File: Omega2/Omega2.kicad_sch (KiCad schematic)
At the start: 6 parts, among them SW1 SW_DIP_x01, U1 Omega2+

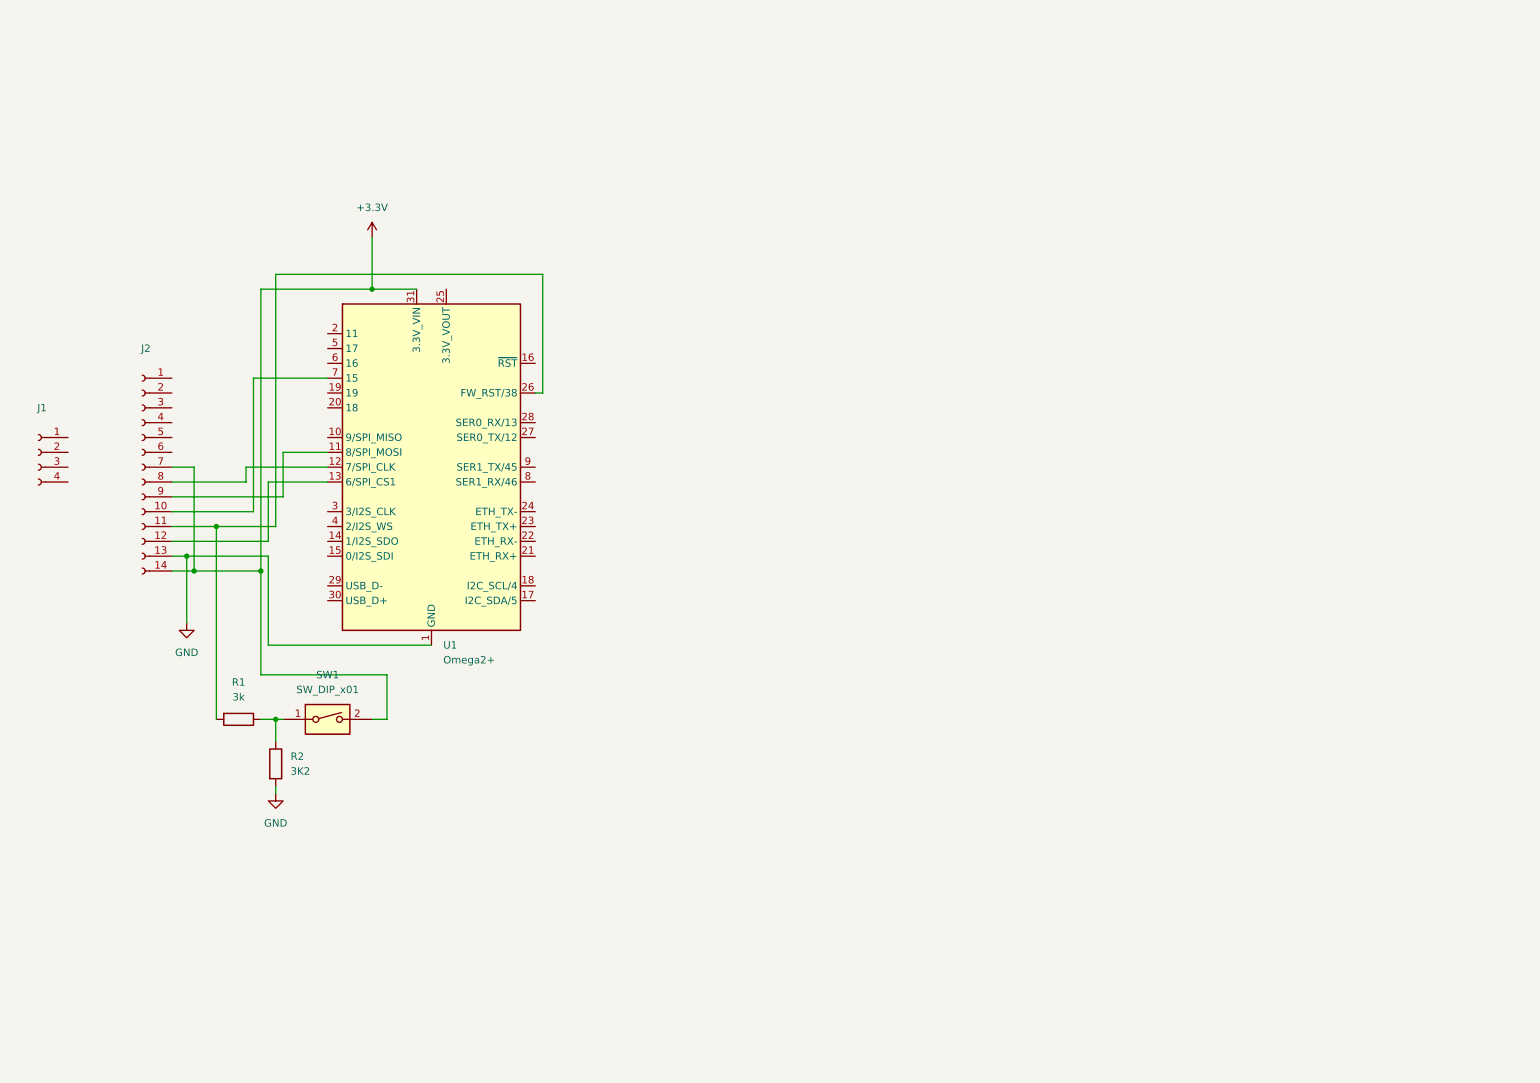
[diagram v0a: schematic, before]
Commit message: Organización display, botón de reset, power flag
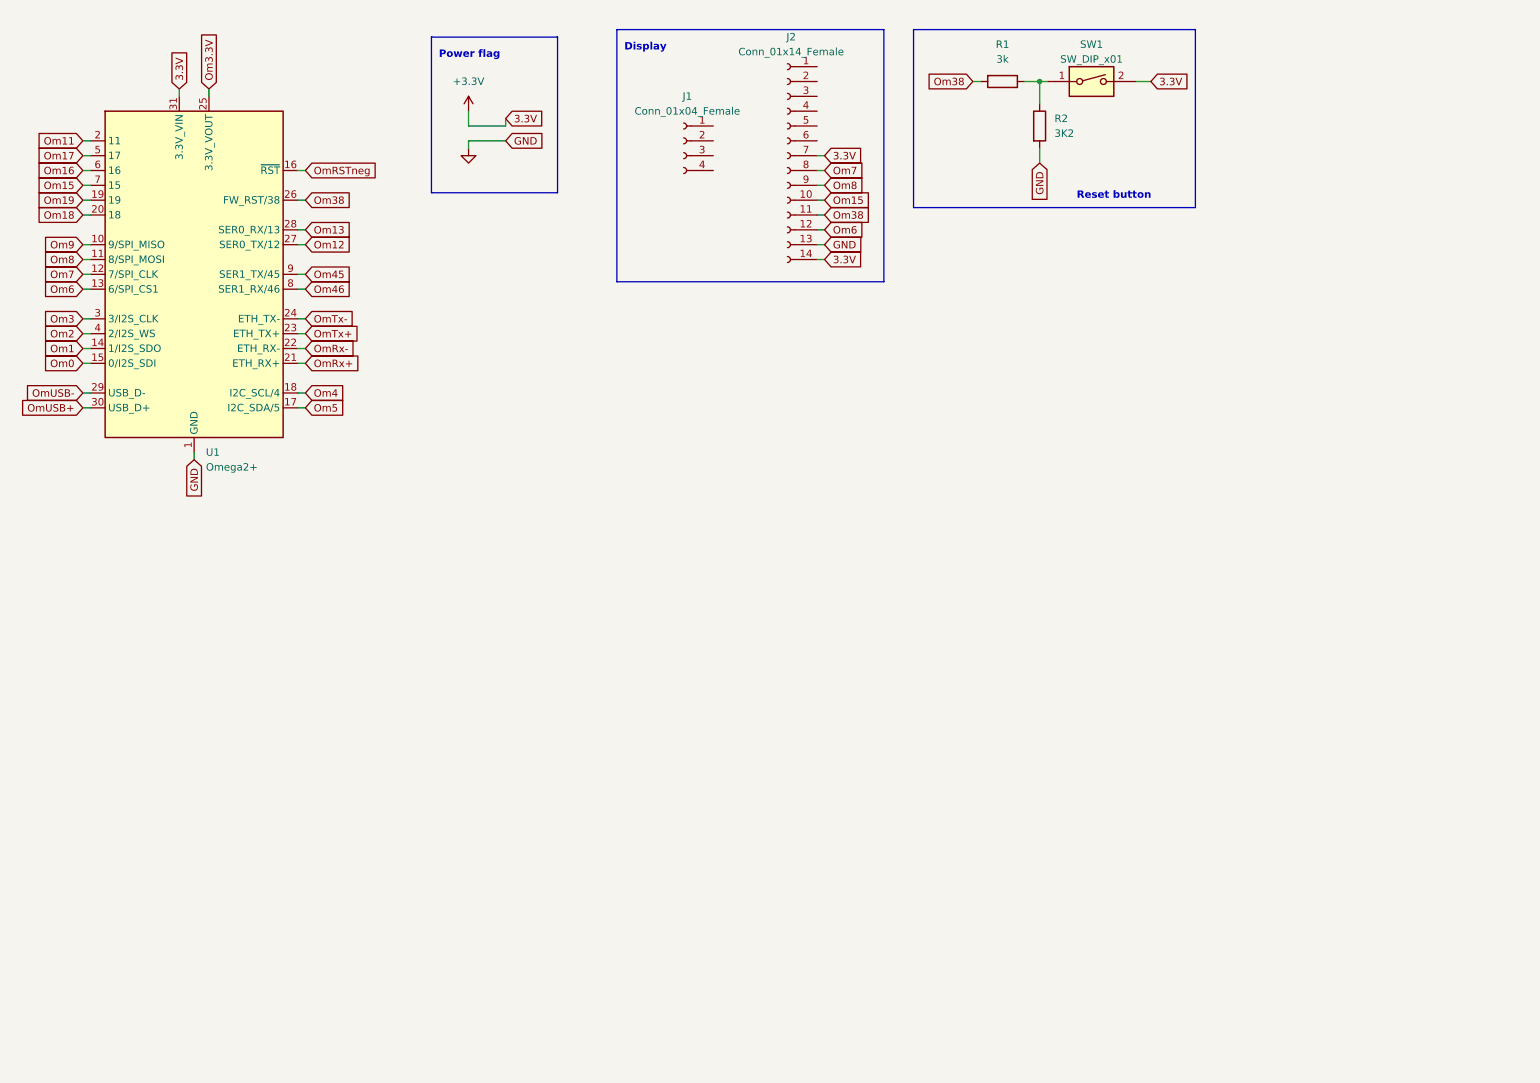
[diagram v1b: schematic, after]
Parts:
- J1: value (none) -> Conn_01x04_Female; footprint (none) -> Connector_PinSocket_2.54mm:PinSocket_1x04_P2.54mm_Vertical
- J2: value (none) -> Conn_01x14_Female; footprint (none) -> Connector_PinSocket_2.54mm:PinSocket_1x14_P2.54mm_Vertical
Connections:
- net Om15: now reaches J2.10 (Pin_10), U1.7 (15)
- net Om38: now reaches J2.11 (Pin_11), R1.2, U1.26 (FW_RST/38)
- net Om6: now reaches J2.12 (Pin_12), U1.13 (6/SPI_CS1)
- net Om7: now reaches J2.8 (Pin_8), U1.12 (7/SPI_CLK)
- net Om8: now reaches J2.9 (Pin_9), U1.11 (8/SPI_MOSI)
- net Om9: now reaches U1.10 (9/SPI_MISO)
- net Om1: now reaches U1.14 (1/I2S_SDO)
- net Om0: now reaches U1.15 (0/I2S_SDI)
- net OmRSTneg: now reaches U1.16 (~{RST})
- net Om5: now reaches U1.17 (I2C_SDA/5)
- net Om4: now reaches U1.18 (I2C_SCL/4)
- net Om19: now reaches U1.19
- net Om11: now reaches U1.2 (11)
- net Om18: now reaches U1.20 (18)
- net OmRx+: now reaches U1.21 (ETH_RX+)
- net OmRx-: now reaches U1.22 (ETH_RX-)
- net OmTx+: now reaches U1.23 (ETH_TX+)
- net OmTx-: now reaches U1.24 (ETH_TX-)
- net Om3.3V: now reaches U1.25 (3.3V_VOUT)
- net Om12: now reaches U1.27 (SER0_TX/12)
- net Om13: now reaches U1.28 (SER0_RX/13)
- net OmUSB-: now reaches U1.29 (USB_D-)
- net Om3: now reaches U1.3 (3/I2S_CLK)
- net OmUSB+: now reaches U1.30 (USB_D+)
- net Om2: now reaches U1.4 (2/I2S_WS)
- net Om17: now reaches U1.5 (17)
- net Om16: now reaches U1.6 (16)
- net Om46: now reaches U1.8 (SER1_RX/46)
- net Om45: now reaches U1.9 (SER1_TX/45)
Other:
- note added: "Display"
- note added: "Power flag"
- note added: "Reset button"
- moved on the sheet: J1, J2, R1, R2, SW1, U1

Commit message: Adicion botones
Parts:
- added C? (x2): 100n, Capacitor_SMD:C_0805_2012Metric_Pad1.18x1.45mm_HandSolder, symbol Device:C
- added R? (x2): 5.1k, Resistor_SMD:R_0805_2012Metric_Pad1.20x1.40mm_HandSolder, symbol Device:R
- added R? (x2): 51k, Resistor_SMD:R_0805_2012Metric_Pad1.20x1.40mm_HandSolder, symbol Device:R
- added SW? (x2): BT, Button_Switch_SMD:SW_SPST_EVQQ2, symbol Switch:SW_Push
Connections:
- net +3V3: now also R?.2, R?.2
- net GND: now also C?.1, C?.1, SW?.2, SW?.2
- net Om16: now also C?.2, R?.1, R?.1
- net Om17: now also C?.2, R?.1, R?.1
- new net: R?.2, SW?.1 (x2)
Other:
- note added: "Botones"

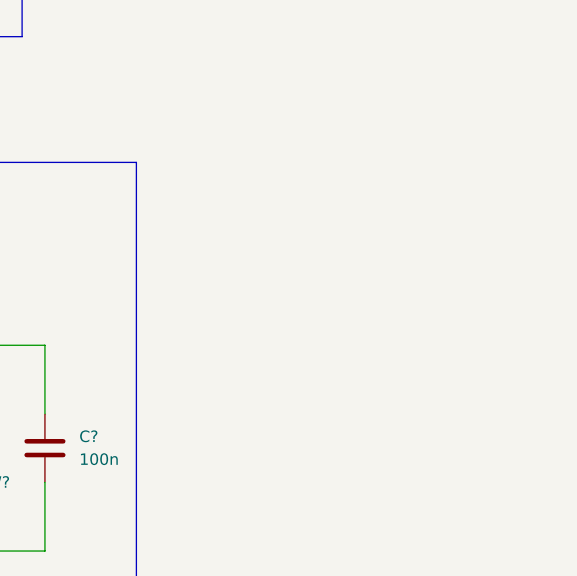
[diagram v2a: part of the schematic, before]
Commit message: Adición Teclado
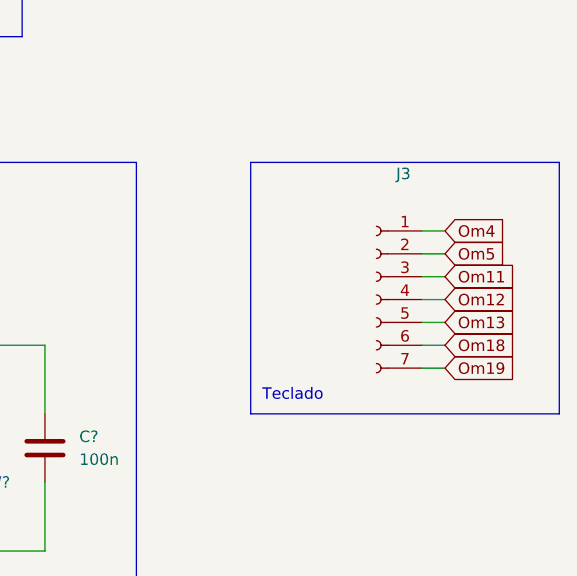
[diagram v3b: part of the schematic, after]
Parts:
- added J3: (no value), symbol Connector:Conn_01x07_Female
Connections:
- net Om11: now also J3.3 (Pin_3)
- net Om12: now also J3.4 (Pin_4)
- net Om13: now also J3.5 (Pin_5)
- net Om18: now also J3.6 (Pin_6)
- net Om19: now also J3.7 (Pin_7)
- net Om4: now also J3.1 (Pin_1)
- net Om5: now also J3.2 (Pin_2)
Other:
- note added: "Teclado"
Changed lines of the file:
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@@
   (junction (at 160.02 93.98) (diameter 0) (color 0 0 0 0)
   )
+  (wire (pts (xy 213.36 86.36) (xy 215.9 86.36))
+    (stroke (width 0) (type default) (color 0 0 0 0))
+  )
   (wire (pts (xy 97.79 33.02) (xy 104.14 33.02))
     (stroke (width 0) (type default) (color 0 0 0 0))
@@
     (stroke (width 0) (type default) (color 0 0 0 0))
   )
+  (wire (pts (xy 213.36 88.9) (xy 215.9 88.9))
+    (stroke (width 0) (type default) (color 0 0 0 0))
+  )
   (wire (pts (xy 53.34 26.67) (xy 53.34 27.94))
     (stroke (width 0) (type default) (color 0 0 0 0))
@@
     (stroke (width 0) (type default) (color 0 0 0 0))
   )
+  (wire (pts (xy 213.36 91.44) (xy 215.9 91.44))
+    (stroke (width 0) (type default) (color 0 0 0 0))
+  )
+  (wire (pts (xy 213.36 93.98) (xy 215.9 93.98))
+    (stroke (width 0) (type default) (color 0 0 0 0))
+  )
+  (wire (pts (xy 213.36 81.28) (xy 215.9 81.28))
+    (stroke (width 0) (type default) (color 0 0 0 0))
+  )
   (wire (pts (xy 69.85 50.8) (xy 68.58 50.8))
     (stroke (width 0) (type default) (color 0 0 0 0))
@@
     (stroke (width 0) (type default) (color 0 0 0 0))
   )
+  (polyline (pts (xy 228.6 101.6) (xy 194.31 101.6))
+    (stroke (width 0) (type default) (color 0 0 0 0))
+  )
   (polyline (pts (xy 109.22 73.66) (xy 181.61 73.66))
     (stroke (width 0) (type default) (color 0 0 0 0))
@@
     (stroke (width 0) (type default) (color 0 0 0 0))
   )
+  (wire (pts (xy 213.36 96.52) (xy 215.9 96.52))
+    (stroke (width 0) (type default) (color 0 0 0 0))
+  )
   (polyline (pts (xy 168.91 16.51) (xy 168.91 59.69))
     (stroke (width 0) (type default) (color 0 0 0 0))
@@
     (stroke (width 0) (type default) (color 0 0 0 0))
   )
+  (wire (pts (xy 213.36 83.82) (xy 215.9 83.82))
+    (stroke (width 0) (type default) (color 0 0 0 0))
+  )
   (wire (pts (xy 160.02 93.98) (xy 160.02 96.52))
     (stroke (width 0) (type default) (color 0 0 0 0))
@@
     (stroke (width 0) (type default) (color 0 0 0 0))
   )
+  (polyline (pts (xy 194.31 73.66) (xy 228.6 73.66))
+    (stroke (width 0) (type default) (color 0 0 0 0))
+  )
   (wire (pts (xy 195.58 25.4) (xy 196.85 25.4))
     (stroke (width 0) (type default) (color 0 0 0 0))
   )
+  (polyline (pts (xy 228.6 73.66) (xy 228.6 101.6))
+    (stroke (width 0) (type default) (color 0 0 0 0))
+  )
   (wire (pts (xy 128.27 93.98) (xy 139.7 93.98))
+    (stroke (width 0) (type default) (color 0 0 0 0))
+  )
+  (polyline (pts (xy 194.31 101.6) (xy 194.31 73.66))
     (stroke (width 0) (type default) (color 0 0 0 0))
   )
@@
     (effects (font (size 1.27 1.27)) (justify left bottom))
   )
+  (text "Teclado\n" (at 195.58 100.33 0)
+    (effects (font (size 1.27 1.27)) (justify left bottom))
+  )
   (text "Display" (at 124.46 20.32 0)
     (effects (font (size 1.27 1.27) (thickness 0.254) bold) (justify left bottom))
@@
     )
   )
+  (global_label "Om19" (shape input) (at 215.9 96.52 0) (fields_autoplaced)
+    (effects (font (size 1.27 1.27)) (justify left))
+    (property "Intersheet References" "${INTERSHEET_REFS}" (id 0) (at 223.756 96.4406 0)
+      (effects (font (size 1.27 1.27)) (justify left) hide)
+    )
+  )
+  (global_label "Om13" (shape input) (at 215.9 91.44 0) (fields_autoplaced)
+    (effects (font (size 1.27 1.27)) (justify left))
+    (property "Intersheet References" "${INTERSHEET_REFS}" (id 0) (at 223.756 91.3606 0)
+      (effects (font (size 1.27 1.27)) (justify left) hide)
+    )
+  )
   (global_label "Om3" (shape input) (at 31.75 66.04 180) (fields_autoplaced)
     (effects (font (size 1.27 1.27)) (justify right))
@@
     )
   )
+  (global_label "Om12" (shape input) (at 215.9 88.9 0) (fields_autoplaced)
+    (effects (font (size 1.27 1.27)) (justify left))
+    (property "Intersheet References" "${INTERSHEET_REFS}" (id 0) (at 223.756 88.8206 0)
+      (effects (font (size 1.27 1.27)) (justify left) hide)
+    )
+  )
   (global_label "OmUSB-" (shape input) (at 31.75 78.74 180) (fields_autoplaced)
     (effects (font (size 1.27 1.27)) (justify right))
@@
     )
   )
+  (global_label "Om5" (shape input) (at 215.9 83.82 0) (fields_autoplaced)
+    (effects (font (size 1.27 1.27)) (justify left))
+    (property "Intersheet References" "${INTERSHEET_REFS}" (id 0) (at 222.5464 83.7406 0)
+      (effects (font (size 1.27 1.27)) (justify left) hide)
+    )
+  )
   (global_label "Om7" (shape input) (at 31.75 58.42 180) (fields_autoplaced)
     (effects (font (size 1.27 1.27)) (justify right))
@@
     )
   )
+  (global_label "Om18" (shape input) (at 215.9 93.98 0) (fields_autoplaced)
+    (effects (font (size 1.27 1.27)) (justify left))
+    (property "Intersheet References" "${INTERSHEET_REFS}" (id 0) (at 223.756 93.9006 0)
+      (effects (font (size 1.27 1.27)) (justify left) hide)
+    )
+  )
   (global_label "Om6" (shape input) (at 31.75 60.96 180) (fields_autoplaced)
     (effects (font (size 1.27 1.27)) (justify right))
@@
     )
   )
+  (global_label "Om11" (shape input) (at 215.9 86.36 0) (fields_autoplaced)
+    (effects (font (size 1.27 1.27)) (justify left))
+    (property "Intersheet References" "${INTERSHEET_REFS}" (id 0) (at 223.756 86.2806 0)
+      (effects (font (size 1.27 1.27)) (justify left) hide)
+    )
+  )
   (global_label "3.3V" (shape input) (at 158.75 55.88 0) (fields_autoplaced)
     (effects (font (size 1.27 1.27)) (justify left))
     (property "Intersheet References" "${INTERSHEET_REFS}" (id 0) (at 165.2755 55.8006 0)
+      (effects (font (size 1.27 1.27)) (justify left) hide)
+    )
+  )
+  (global_label "Om4" (shape input) (at 215.9 81.28 0) (fields_autoplaced)
+    (effects (font (size 1.27 1.27)) (justify left))
+    (property "Intersheet References" "${INTERSHEET_REFS}" (id 0) (at 222.5464 81.2006 0)
       (effects (font (size 1.27 1.27)) (justify left) hide)
     )
@@
     (pin "2")
   )
+  (symbol (lib_id "Connector:Conn_01x07_Female") (at 208.28 88.9 0) (mirror y) (unit 1)
+    (in_bom yes) (on_board yes)
+    (property "Reference" "J3" (id 0) (at 212.09 74.93 0)
+      (effects (font (size 1.27 1.27)) (justify left))
+    )
+    (property "Value" "" (id 1) (at 215.9 77.47 0)
+      (effects (font (size 1.27 1.27)) (justify left))
+    )
+    (property "Footprint" "" (id 2) (at 208.28 88.9 0)
+      (effects (font (size 1.27 1.27)) hide)
+    )
+    (property "Datasheet" "~" (id 3) (at 208.28 88.9 0)
+      (effects (font (size 1.27 1.27)) hide)
+    )
+    (pin "1")
+    (pin "2")
+    (pin "3")
+    (pin "4")
+    (pin "5")
+    (pin "6")
+    (pin "7")
+  )
   (symbol (lib_id "Device:C") (at 139.7 105.41 180) (unit 1)
     (in_bom yes) (on_board yes) (fields_autoplaced)
@@
       (reference "J2") (unit 1) (value "Conn_01x14_Female") (footprint "Connector_PinSocket_2.54mm:PinSocket_1x14_P2.54mm_Vertical")
     )
+    (path "/6f4c06dc-e24f-4f66-84b3-0dc17375c4c4"
+      (reference "J3") (unit 1) (value "Conn_01x07_Female") (footprint "Connector_PinSocket_2.54mm:PinSocket_1x07_P2.54mm_Vertical")
+    )
     (path "/5c9c653f-d9af-4652-b5e1-fa03e9583f41"

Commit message: edición pulsadores
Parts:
- J3: value (none) -> Conn_01x07_Female; footprint (none) -> Connector_PinSocket_2.54mm:PinSocket_1x07_P2.54mm_Vertical
- SW2, SW3: renamed from SW?; value BT -> (none); footprint Button_Switch_SMD:SW_SPST_EVQQ2 -> (none)
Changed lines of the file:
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@@
   (symbol (lib_id "Switch:SW_Push") (at 160.02 110.49 270) (unit 1)
     (in_bom yes) (on_board yes) (fields_autoplaced)
-    (property "Reference" "SW?" (id 0) (at 163.83 109.2199 90)
-      (effects (font (size 1.27 1.27)) (justify left))
-    )
-    (property "Value" "BT" (id 1) (at 163.83 111.7599 90)
-      (effects (font (size 1.27 1.27)) (justify left))
-    )
-    (property "Footprint" "Button_Switch_SMD:SW_SPST_EVQQ2" (id 2) (at 165.1 110.49 0)
+    (property "Reference" "SW2" (id 0) (at 163.83 109.2199 90)
+      (effects (font (size 1.27 1.27)) (justify left))
+    )
+    (property "Value" "" (id 1) (at 163.83 111.7599 90)
+      (effects (font (size 1.27 1.27)) (justify left))
+    )
+    (property "Footprint" "" (id 2) (at 165.1 110.49 0)
       (effects (font (size 1.27 1.27)) hide)
     )
@@
       (effects (font (size 1.27 1.27)) (justify left))
     )
-    (property "Value" "" (id 1) (at 215.9 77.47 0)
-      (effects (font (size 1.27 1.27)) (justify left))
-    )
-    (property "Footprint" "" (id 2) (at 208.28 88.9 0)
+    (property "Value" "Conn_01x07_Female" (id 1) (at 215.9 77.47 0)
+      (effects (font (size 1.27 1.27)) (justify left))
+    )
+    (property "Footprint" "Connector_PinSocket_2.54mm:PinSocket_1x07_P2.54mm_Vertical" (id 2) (at 208.28 88.9 0)
       (effects (font (size 1.27 1.27)) hide)
     )
@@
   (symbol (lib_id "Switch:SW_Push") (at 128.27 110.49 270) (unit 1)
     (in_bom yes) (on_board yes) (fields_autoplaced)
-    (property "Reference" "SW?" (id 0) (at 132.08 109.2199 90)
-      (effects (font (size 1.27 1.27)) (justify left))
-    )
-    (property "Value" "BT" (id 1) (at 132.08 111.7599 90)
-      (effects (font (size 1.27 1.27)) (justify left))
-    )
-    (property "Footprint" "Button_Switch_SMD:SW_SPST_EVQQ2" (id 2) (at 133.35 110.49 0)
+    (property "Reference" "SW3" (id 0) (at 132.08 109.2199 90)
+      (effects (font (size 1.27 1.27)) (justify left))
+    )
+    (property "Value" "" (id 1) (at 132.08 111.7599 90)
+      (effects (font (size 1.27 1.27)) (justify left))
+    )
+    (property "Footprint" "" (id 2) (at 133.35 110.49 0)
       (effects (font (size 1.27 1.27)) hide)
     )
@@
     )
     (path "/0a3cbae7-b160-4bf5-bc29-b843867e2bbd"
-      (reference "SW?") (unit 1) (value "BT") (footprint "Button_Switch_SMD:SW_SPST_EVQQ2")
+      (reference "SW2") (unit 1) (value "FW") (footprint "TerminalBlock:TerminalBlock_Altech_AK300-2_P5.00mm")
     )
     (path "/f0305a19-1293-46c9-9810-aa49b8dab8a4"
-      (reference "SW?") (unit 1) (value "BT") (footprint "Button_Switch_SMD:SW_SPST_EVQQ2")
+      (reference "SW3") (unit 1) (value "BW") (footprint "TerminalBlock:TerminalBlock_Altech_AK300-2_P5.00mm")
     )
     (path "/1c052668-6749-425a-9a77-35f046c8aa39"
